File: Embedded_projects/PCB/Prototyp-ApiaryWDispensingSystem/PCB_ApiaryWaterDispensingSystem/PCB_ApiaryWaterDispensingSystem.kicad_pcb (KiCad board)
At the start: 2 copper layers, 217.3 x 127.3 mm, 255 parts, among them J1 Conn_02x01, J10 Conn_02x19_Odd_Even, J11 Conn_02x01, J12 Conn_02x01, J13 Conn_01x03, J14 Conn_01x02, J15 Conn_01x02, J16 Conn_02x01, J17 MSD-1-A, J18 Conn_01x02, J19 Conn_01x08, J2 Conn_01x04, J20 USB_B_Micro, J21 Conn_02x01, J3 Conn_02x01, J4 Conn_01x06, J5 Conn_01x03_Male, J6 Conn_02x01, J7 Conn_02x19_Odd_Even, J8 Conn_01x05_Male, J9 Conn_01x04_Male, Q1 Q_PMOS_GSD, Q2 Q_NPN_BEC, SW2 SW_Push, SW3 SW_Push, SW4 SW_Push, SW5 SW_Push, SW6 SW_Push, U1 STM32F411RETx, U10 LD3985M33R_SOT23, U11 STM32F103CBTx, U12 LD39050PU33, U2 24LC32, U3 DS3231M, U4 INA219AxD, U5 BME280, U6 INA219AxD, U7 drv8835, U8 LD1117S50TR_SOT223, U9 STS7PF30L, X1 Crystal, Y2 Crystal_GND23_Small, Y3 Crystal

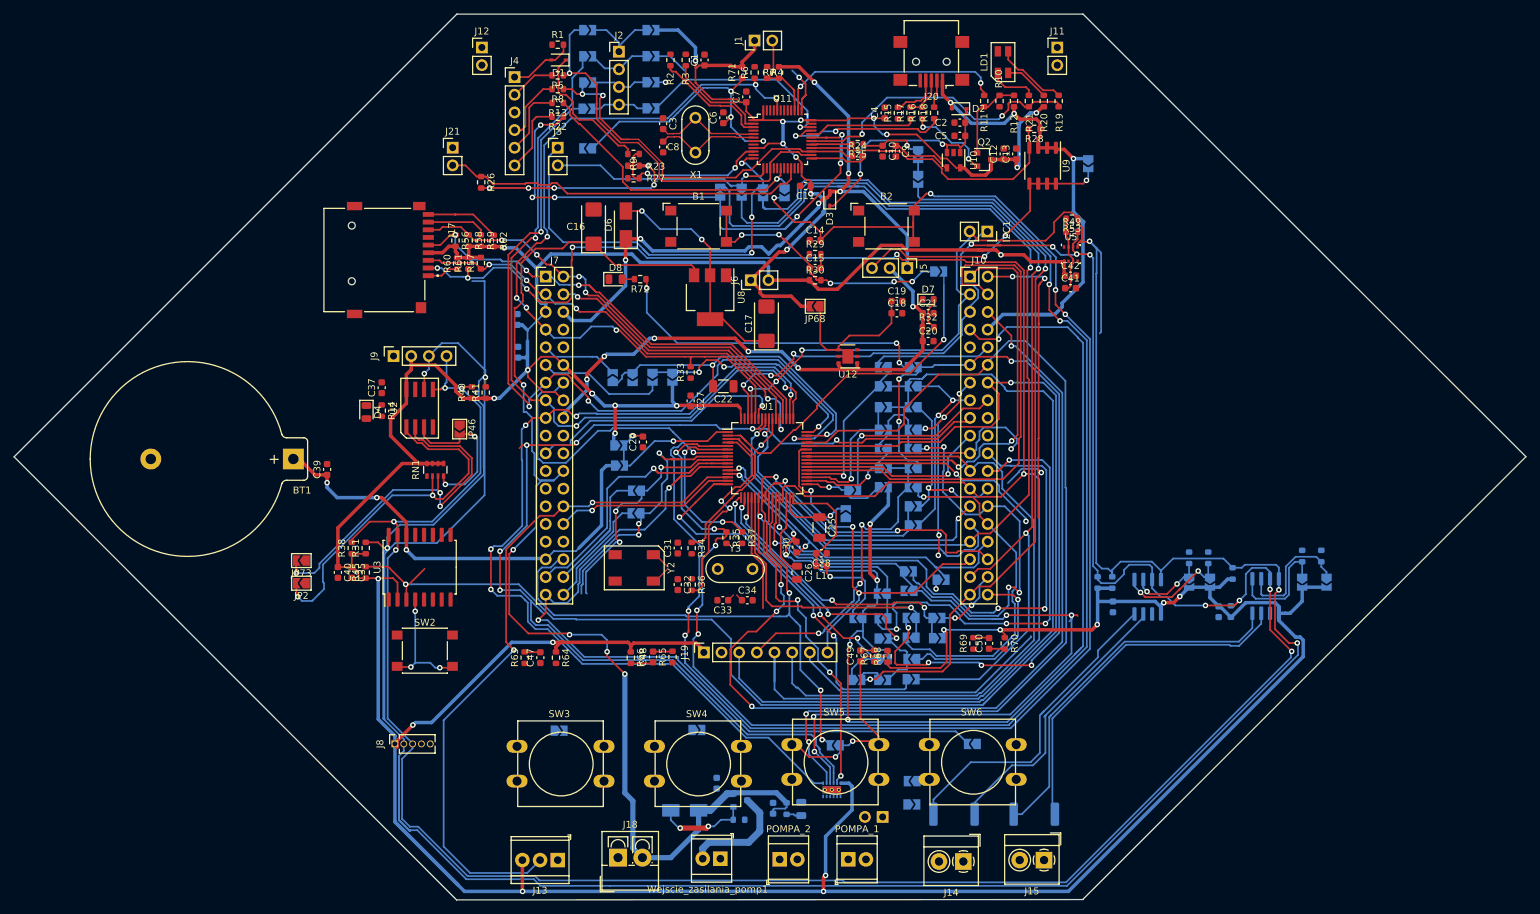
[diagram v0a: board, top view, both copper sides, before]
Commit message: update html in readme.RST and improved PCb #3
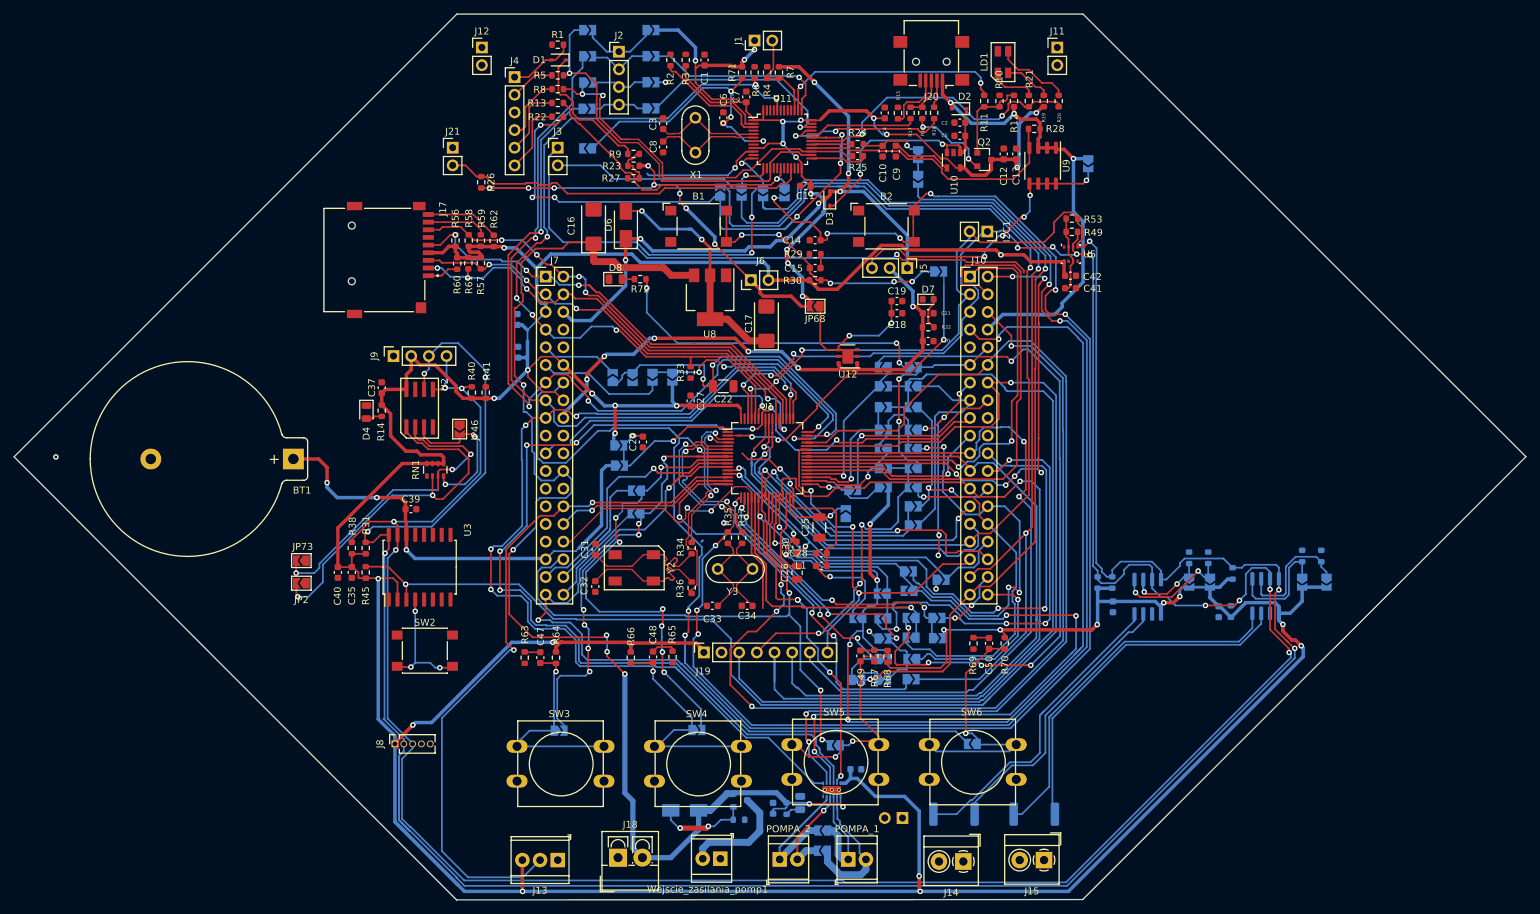
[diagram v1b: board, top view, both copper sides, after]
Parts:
- moved C44 20.1 mm to (164.5, 134.6), turned to 0 degrees
- moved JP66 14.7 mm to (159.8, 143.4)
- moved JP52 14.5 mm to (159.7, 146.3), turned to 180 degrees
- moved C39 13.3 mm to (100.5, 97.2), turned to 0 degrees
- moved C32 11.9 mm to (127.0, 108.3)
- moved C31 11.8 mm to (127.1, 103.0)
- moved J16 2.85 mm to (171.2, 141.6)
- moved C33 1.70 mm to (143.9, 111.1)
- moved C45 0.86 mm to (156.5, 139.4)
- moved C34 0.80 mm to (148.9, 111.1), turned to 180 degrees
- moved R36 0.45 mm to (140.9, 108.5)
- moved R35 0.20 mm to (146.1, 101.3)
- turned C28 to 0 degrees
- turned L1 to 0 degrees
- turned R10 to 270 degrees
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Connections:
- C30 pad 1: GNDA -> GND1
- J10 pad 25: DAT3 -> PB10
- J10 pad 32: GNDA -> GND1
- J19 pad 5: DAT3 -> PB10
- J7 pad 4: PD2 -> DAT3
- JP60 pad 2: GNDA -> GND1
- U1 pad 12: GNDA -> GND1
- U1 pad 29: DAT3 -> PB10
- U1 pad 54: PD2 -> DAT3
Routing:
- net DAT3: track 247.2 -> 64.7 mm, vias 6 -> 3
- net PB10: track 0.00 -> 175.9 mm, vias 0 -> 2
- net PB8: track 519.9 -> 436.1 mm, vias 9 -> 10
- net GNDA: track 51.7 -> 0.00 mm, vias 2 -> 0
- net GND1: track 0.00 -> 50.8 mm, vias 0 -> 2
- net PD2: track 40.0 -> 0.00 mm, vias 1 -> 0
- net Net-(C50-Pad1): track 2.27 -> 37.5 mm, vias 0 -> 1
- net PA4: track 16.6 -> 50.8 mm, vias 0 -> 2
- net PC1: track 39.3 -> 71.7 mm, vias 3 -> 7
- net Net-(C47-Pad1): track 0.00 -> 31.1 mm, vias 0 -> 1
- net Net-(C48-Pad1): track 3.69 -> 34.6 mm, vias 0 -> 1
- net PA9: track 74.1 -> 102.0 mm, vias 1 -> 2
- net VDD: track 657.7 -> 685.5 mm, vias 20 -> 24
- net PC0: track 40.2 -> 66.7 mm, vias 3 -> 7
- net +3V3: track 178.9 -> 203.9 mm, vias 16 -> 23
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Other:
- net class PWR added: clearance 0.2, trace_width 0.4, via_dia 0.8, via_drill 0.4
